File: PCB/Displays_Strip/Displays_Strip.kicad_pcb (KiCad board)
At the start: 2 copper layers, 31 parts, among them J1 Power, J2 ICSP, J3 Comm_I2C, J4 EEPROM_Prog, U1 PIC32MX270F256D-IPT, U12 CAT4104V-GT3, U13 CAT4104V-GT3, U14 CAT4104V-GT3, U15 M95P32-IXMGT/E, U16 LDL1117S33R, Y1 16M

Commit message: Schematic Flash
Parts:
- added C11: 100n, Capacitor_SMD:C_0805_2012Metric, F.Cu at (134.0, 67.0)
- added C12: 100n, Capacitor_SMD:C_0805_2012Metric, F.Cu at (134.0, 47.0)
- added U10: DT010ATFT, Console:Hirose FFC FPC 13 Pin Inverted, F.Cu at (209.1, 125.2)
- added U11: DT010ATFT, Console:Hirose FFC FPC 13 Pin Inverted, F.Cu at (226.1, 125.2)
- added U2: DT010ATFT, Console:Hirose FFC FPC 13 Pin Inverted, F.Cu at (46.0, 124.8)
- added U3: DT010ATFT, Console:Hirose FFC FPC 13 Pin Inverted, F.Cu at (62.0, 124.8)
- added U4: DT010ATFT, Console:Hirose FFC FPC 13 Pin Inverted, F.Cu at (80.1, 124.2)
- added U5: DT010ATFT, Console:Hirose FFC FPC 13 Pin Inverted, F.Cu at (100.1, 124.2)
- added U6: DT010ATFT, Console:Hirose FFC FPC 13 Pin Inverted, F.Cu at (120.1, 126.2)
- added U7: DT010ATFT, Console:Hirose FFC FPC 13 Pin Inverted, F.Cu at (143.2, 126.8)
- added U8: DT010ATFT, Console:Hirose FFC FPC 13 Pin Inverted, F.Cu at (164.1, 126.2)
- added U9: DT010ATFT, Console:Hirose FFC FPC 13 Pin Inverted, F.Cu at (187.1, 125.2)
- moved J1 121.0 mm to (83.0, 27.0)
- moved U16 99.4 mm to (97.0, 29.0), turned to 180 degrees
- moved J3 96.8 mm to (82.0, 60.5), turned to 180 degrees
- moved C2 94.9 mm to (97.0, 37.0)
- moved C1 94.7 mm to (105.0, 29.0), turned to -90 degrees
- moved C10 91.4 mm to (121.0, 39.0), turned to 90 degrees
- moved R10 87.4 mm to (88.1, 61.0), turned to 180 degrees
- moved R9 87.4 mm to (88.1, 58.0), turned to 180 degrees
- moved C9 85.1 mm to (131.0, 39.0), turned to 90 degrees
- moved C3 75.2 mm to (151.1, 42.0), turned to 180 degrees
- moved J4 75.0 mm to (166.0, 42.1)
- moved C8 73.8 mm to (114.0, 57.0), turned to 90 degrees
- moved R5 73.3 mm to (161.0, 43.0), turned to -90 degrees
- moved C4 70.9 mm to (120.0, 57.0), turned to 90 degrees
- moved R4 69.7 mm to (158.0, 43.0), turned to -90 degrees
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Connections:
- J4 pad 1: /MISO_MEM -> +3.3V
- J4 pad 2: /nCS_MEM -> /nHOLD_MEM
- J4 pad 3: +3.3V -> /CLK_MEM
- J4 pad 4: /nCS_MEM -> /MOSI_MEM
- J4 pad 5: /CLK_MEM -> /nCS_MEM
- J4 pad 6: /MOSI_MEM -> /MISO_MEM
- J4 pad 7: /nCS_MEM -> /nW_MEM
- R5 pad 2: /nCS_MEM -> /nHOLD_MEM
- R6 pad 2: /nCS_MEM -> /nW_MEM
- U1 pad 22: /nCS_MEM -> /nHOLD_MEM
- U1 pad 27: /nCS_MEM -> /nW_MEM
- U15 pad 3: /nCS_MEM -> /nW_MEM
- U15 pad 7: /nCS_MEM -> /nHOLD_MEM

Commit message: PCB Displays
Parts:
- added H1: MountingHole, MountingHole:MountingHole_3.2mm_M3, F.Cu at (44.0, 125.0)
- added H2: MountingHole, MountingHole:MountingHole_3.2mm_M3, F.Cu at (267.0, 123.0)
- added H3: MountingHole, MountingHole:MountingHole_3.2mm_M3, F.Cu at (119.0, 125.0)
- added H4: MountingHole, MountingHole:MountingHole_3.2mm_M3, F.Cu at (69.0, 145.0)
- added H5: MountingHole, MountingHole:MountingHole_3.2mm_M3, F.Cu at (194.0, 145.0)
- moved C10 146.4 mm to (238.0, 127.0), turned to 0 degrees
- moved U14 144.6 mm to (260.5, 133.8), turned to 0 degrees
- moved R3 143.3 mm to (263.0, 128.8), turned to 90 degrees
- moved C9 141.1 mm to (238.0, 131.0), turned to 0 degrees
- moved R9 136.1 mm to (206.0, 126.0)
- moved J3 135.7 mm to (202.5, 123.0), turned to 90 degrees
- moved Y1 135.7 mm to (233.0, 131.4), turned to 90 degrees
- moved C8 131.8 mm to (227.5, 124.0), turned to 0 degrees
- moved R7 131.2 mm to (258.8, 127.2)
- moved R10 130.7 mm to (201.5, 126.0), turned to 0 degrees
- moved R8 130.3 mm to (255.8, 126.2), turned to 180 degrees
- moved C12 127.1 mm to (229.0, 131.5), turned to 90 degrees
- moved C6 127.0 mm to (255.8, 128.2), turned to 180 degrees
- moved C4 120.0 mm to (219.5, 124.0), turned to 0 degrees
- moved J1 119.0 mm to (153.3, 123.0), turned to -90 degrees
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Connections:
- J2 pad 4: Net-(J2-Pin_4) -> /PGED
- J2 pad 5: Net-(J2-Pin_5) -> /PGEC
- J4 pad 1: +3.3V -> /CLK_MEM
- J4 pad 2: /nHOLD_MEM -> /MOSI_MEM
- J4 pad 3: /CLK_MEM -> +3.3V
- J4 pad 4: /MOSI_MEM -> /nHOLD_MEM
- J4 pad 5: /nCS_MEM -> /nW_MEM
- J4 pad 7: /nW_MEM -> /nCS_MEM
- U1 pad 11: /MOSI_MEM -> /nHOLD_MEM
- U1 pad 12: unconnected-(U1-RA10-Pad12) -> /nRESET_LCD
- U1 pad 13: unconnected-(U1-RA7-Pad13) -> /D/C_LCD
- U1 pad 19: Net-(J2-Pin_4) -> unconnected-(U1-RA0-Pad19)
- U1 pad 2: /nCS_2 -> /MISO_MEM
- U1 pad 20: Net-(J2-Pin_5) -> unconnected-(U1-RA1-Pad20)
- U1 pad 21: /nCS_MEM -> unconnected-(U1-RB0-Pad21)
- U1 pad 22: /nHOLD_MEM -> /SDA_LCD
- U1 pad 25: unconnected-(U1-RC0-Pad25) -> /nCS_7
- U1 pad 26: /MISO_MEM -> /nCS_8
- U1 pad 27: /nW_MEM -> /nCS_9
- U1 pad 3: /nCS_1 -> /nW_MEM
- U1 pad 34: /nCS_9 -> /nCS_0
- U1 pad 35: /nCS_8 -> /nCS_1
- U1 pad 36: /nCS_7 -> /nCS_2
- U1 pad 37: /nCS_6 -> /nCS_3
- U1 pad 38: /nCS_5 -> /nCS_4
- U1 pad 4: /nCS_0 -> /MOSI_MEM
- U1 pad 41: /nCS_4 -> /nCS_5
- U1 pad 43: /nCS_3 -> /nCS_6
- U1 pad 5: /nRESET_LCD -> /nCS_MEM
- U1 pad 8: /D/C_LCD -> /PGED
- U1 pad 9: /SDA_LCD -> /PGEC
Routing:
- net +3.3V: track 0.00 -> 846.4 mm, vias 0 -> 22
- net /nRESET_LCD: track 0.00 -> 277.7 mm, vias 0 -> 20
- net /SCK_LCD: track 0.00 -> 269.5 mm
- net /D/C_LCD: track 0.00 -> 268.1 mm, vias 0 -> 20
- net /SDA_LCD: track 0.00 -> 266.2 mm, vias 0 -> 2
- net /nCS_0: track 0.00 -> 210.9 mm, vias 0 -> 2
- net /PWM_LCD: track 0.00 -> 208.6 mm, vias 0 -> 2
- net /nCS_1: track 0.00 -> 186.0 mm, vias 0 -> 4
- net /nCS_2: track 0.00 -> 159.2 mm, vias 0 -> 4
- net /nCS_3: track 0.00 -> 132.0 mm, vias 0 -> 4
- net GND: track 0.00 -> 111.2 mm, vias 0 -> 90
- net /nCS_4: track 0.00 -> 103.9 mm, vias 0 -> 4
- net /nCS_5: track 0.00 -> 77.3 mm, vias 0 -> 4
- net /CLK_MEM: track 0.00 -> 59.3 mm
- net Net-(J2-Pin_1): track 0.00 -> 53.8 mm, vias 0 -> 2
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- added copper zone on B.Cu, net GND
- added copper zone on F.Cu, net GND
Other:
- board outline added: 250 x 30 mm

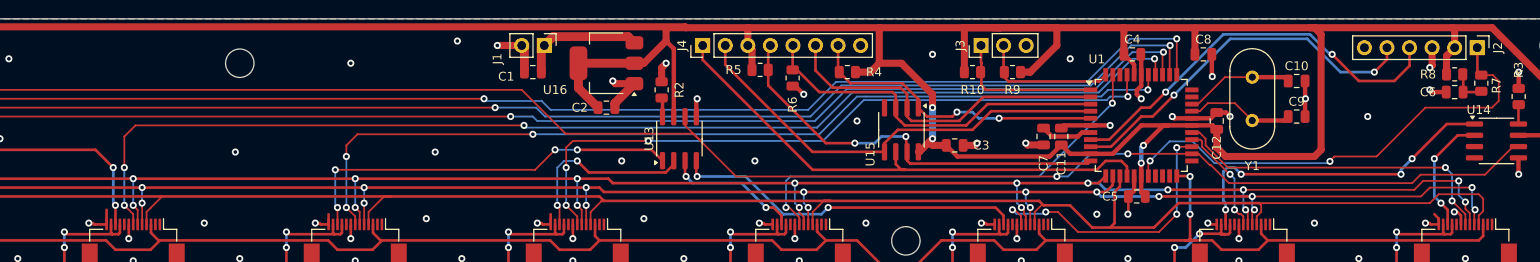
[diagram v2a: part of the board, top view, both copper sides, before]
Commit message: Fader Breakout Board
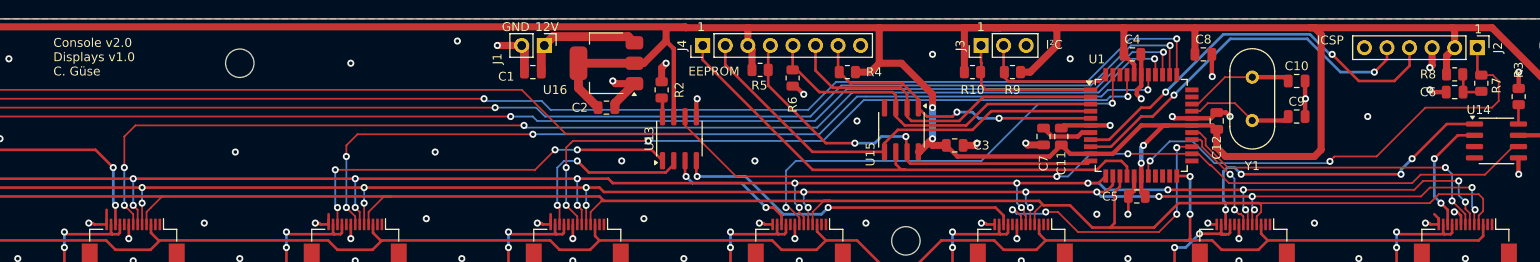
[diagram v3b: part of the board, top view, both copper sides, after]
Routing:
- net /nCS_6: track 49.3 -> 50.0 mm
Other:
- board text added: "1"
- board text added: "12V"
- board text added: "Console v2.0 Displays v1.0 C. Güse"
- board text added: "EEPROM"
- board text added: "GND"
- board text added: "ICSP"
- board text added: "I²C"
